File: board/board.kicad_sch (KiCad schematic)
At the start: 34 parts, among them J1 Conn_01x10_Pin, J2 Conn_01x10, J4 Conn_01x02, J5 Conn_01x06, J6 Conn_01x04, J7 Conn_01x30, U2 nPM1300-QEAA, U3 MDBT50Q-P1MV2, Y1 32k Hz

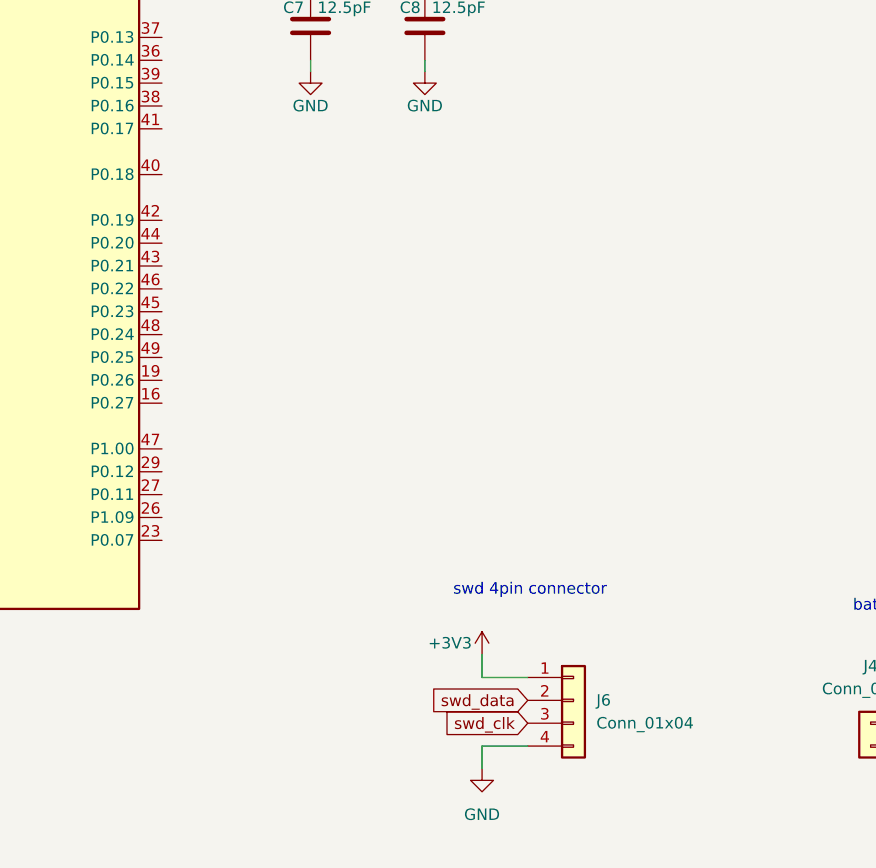
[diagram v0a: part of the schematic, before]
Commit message: board: sch fix swd connect with new footprint
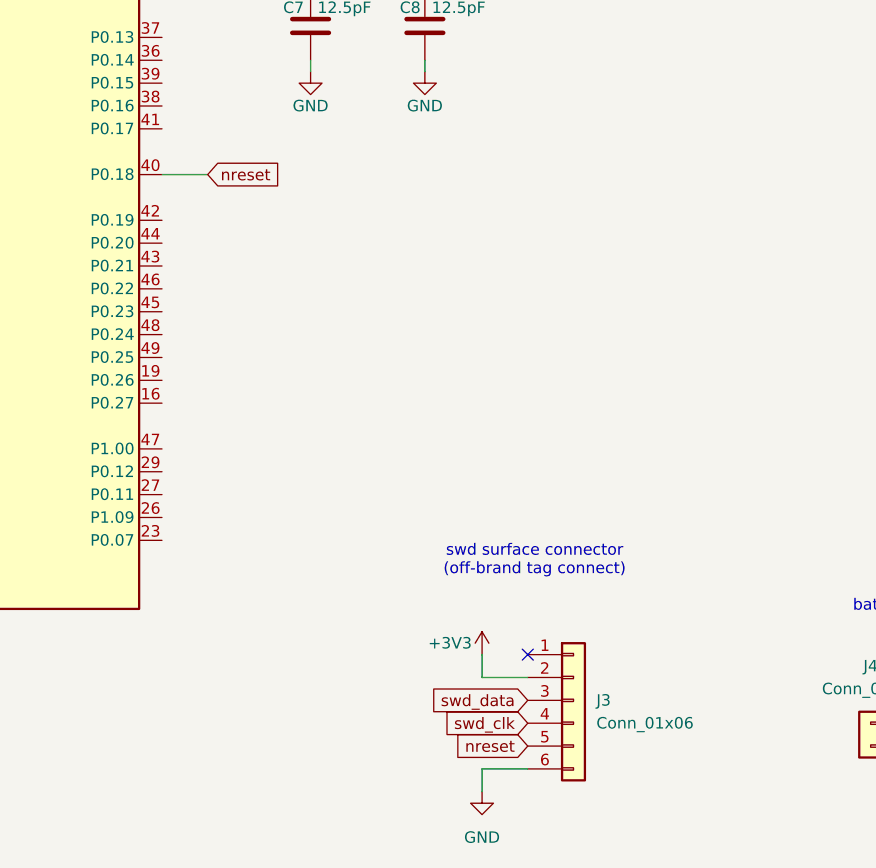
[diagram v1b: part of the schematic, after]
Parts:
- removed J6: Conn_01x04, symbol Connector_Generic:Conn_01x04
- added J3: Conn_01x06, phiboard:swd_pad, symbol Connector_Generic:Conn_01x06
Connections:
- net +3V3: now also J3.2 (Pin_2)
- net GND: now also J3.6 (Pin_6)
- net swd_clk: now also J3.4 (Pin_4)
- net swd_data: now also J3.3 (Pin_3)
- net nreset: now reaches U3.40 (P0.18)
- net nreset: now also J3.5 (Pin_5)
- no-connect marks 12 -> 13
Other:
- note added: "swd surface connector (off-brand tag connect)"
- note removed: "swd 4pin connector"
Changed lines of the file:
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@@
 		)
 	)
-	(text "swd 4pin connector"
+	(text "swd surface connector\n(off-brand tag connect)"
 		(exclude_from_sim no)
-		(at 164.084 250.698 0)
+		(at 164.592 247.396 0)
 		(effects
 			(font
@@
 	)
 	(no_connect
+		(at 163.83 257.81)
+	)
+	(no_connect
 		(at 290.83 53.34)
 	)
@@
 	(wire
 		(pts
+			(xy 128.27 204.47) (xy 123.19 204.47)
+		)
+		(stroke
+			(width 0)
+			(type default)
+		)
+	)
+	(wire
+		(pts
 			(xy 262.89 257.81) (xy 254 257.81)
 		)
@@
 	(wire
 		(pts
-			(xy 158.75 270.51) (xy 158.75 267.97)
+			(xy 158.75 273.05) (xy 158.75 270.51)
 		)
 		(stroke
@@
 	(wire
 		(pts
-			(xy 158.75 267.97) (xy 163.83 267.97)
+			(xy 158.75 270.51) (xy 163.83 270.51)
 		)
 		(stroke
@@
 		)
 	)
+	(global_label "nreset"
+		(shape input)
+		(at 128.27 204.47 0)
+		(fields_autoplaced yes)
+		(effects
+			(font
+				(size 1.27 1.27)
+			)
+			(justify left)
+		)
+		(property "Intersheetrefs" "${INTERSHEET_REFS}"
+			(at 137.1214 204.47 0)
+			(effects
+				(font
+					(size 1.27 1.27)
+				)
+				(justify left)
+				(hide yes)
+			)
+		)
+	)
 	(global_label "usbd-"
 		(shape input)
@@
 		)
 	)
+	(global_label "nreset"
+		(shape input)
+		(at 163.83 267.97 180)
+		(fields_autoplaced yes)
+		(effects
+			(font
+				(size 1.27 1.27)
+			)
+			(justify right)
+		)
+		(property "Intersheetrefs" "${INTERSHEET_REFS}"
+			(at 154.9786 267.97 0)
+			(effects
+				(font
+					(size 1.27 1.27)
+				)
+				(justify right)
+				(hide yes)
+			)
+		)
+	)
 	(global_label "sclk"
 		(shape input)
@@
 	)
 	(symbol
+		(lib_id "Connector_Generic:Conn_01x06")
+		(at 168.91 262.89 0)
+		(unit 1)
+		(exclude_from_sim no)
+		(in_bom yes)
+		(on_board yes)
+		(dnp no)
+		(fields_autoplaced yes)
+		(property "Reference" "J3"
+			(at 171.45 262.8899 0)
+			(effects
+				(font
+					(size 1.27 1.27)
+				)
+				(justify left)
+			)
+		)
+		(property "Value" "Conn_01x06"
+			(at 171.45 265.4299 0)
+			(effects
+				(font
+					(size 1.27 1.27)
+				)
+				(justify left)
+			)
+		)
+		(property "Footprint" "phiboard:swd_pad"
+			(at 168.91 262.89 0)
+			(effects
+				(font
+					(size 1.27 1.27)
+				)
+				(hide yes)
+			)
+		)
+		(property "Datasheet" "~"
+			(at 168.91 262.89 0)
+			(effects
+				(font
+					(size 1.27 1.27)
+				)
+				(hide yes)
+			)
+		)
+		(property "Description" "Generic connector, single row, 01x06, script generated (kicad-library-utils/schlib/autogen/connector/)"
+			(at 168.91 262.89 0)
+			(effects
+				(font
+					(size 1.27 1.27)
+				)
+				(hide yes)
+			)
+		)
+		(pin "4"
+		)
+		(pin "3"
+		)
+		(pin "2"
+		)
+		(pin "1"
+		)
+		(pin "6"
+		)
+		(pin "5"
+		)
+		(instances
+			(project ""
+				(path "/0bf1fdd4-5a89-4735-8383-190e40fb0179"
+					(reference "J3")
+					(unit 1)
+				)
+			)
+		)
+	)
+	(symbol
 		(lib_id "Device:LED")
 		(at 281.94 69.85 180)
@@
 	)
 	(symbol
-		(lib_id "Connector_Generic:Conn_01x04")
-		(at 168.91 262.89 0)
-		(unit 1)
-		(exclude_from_sim no)
-		(in_bom yes)
-		(on_board yes)
-		(dnp no)
-		(property "Reference" "J6"
-			(at 171.45 262.8899 0)
-			(effects
-				(font
-					(size 1.27 1.27)
-				)
-				(justify left)
-			)
-		)
-		(property "Value" "Conn_01x04"
-			(at 171.45 265.4299 0)
-			(effects
-				(font
-					(size 1.27 1.27)
-				)
-				(justify left)
-			)
-		)
-		(property "Footprint" ""
-			(at 168.91 262.89 0)
-			(effects
-				(font
-					(size 1.27 1.27)
-				)
-				(hide yes)
-			)
-		)
-		(property "Datasheet" "~"
-			(at 168.91 262.89 0)
-			(effects
-				(font
-					(size 1.27 1.27)
-				)
-				(hide yes)
-			)
-		)
-		(property "Description" "Generic connector, single row, 01x04, script generated (kicad-library-utils/schlib/autogen/connector/)"
-			(at 168.91 262.89 0)
-			(effects
-				(font
-					(size 1.27 1.27)
-				)
-				(hide yes)
-			)
-		)
-		(pin "3"
-		)
-		(pin "2"
-		)
-		(pin "4"
-		)
-		(pin "1"
-		)
-		(instances
-			(project ""
-				(path "/0bf1fdd4-5a89-4735-8383-190e40fb0179"
-					(reference "J6")
-					(unit 1)
-				)
-			)
-		)
-	)
-	(symbol
 		(lib_id "Device:R")
 		(at 283.21 83.82 90)
@@
 	(symbol
 		(lib_id "power:GND")
-		(at 158.75 270.51 0)
+		(at 158.75 273.05 0)
 		(unit 1)
 		(exclude_from_sim no)
@@
 		(fields_autoplaced yes)
 		(property "Reference" "#PWR024"
-			(at 158.75 276.86 0)
+			(at 158.75 279.4 0)
 			(effects
 				(font
@@
 		)
 		(property "Value" "GND"
-			(at 158.75 275.59 0)
+			(at 158.75 278.13 0)
 			(effects
 				(font
@@
 		)
 		(property "Footprint" ""
-			(at 158.75 270.51 0)
+			(at 158.75 273.05 0)
 			(effects
 				(font
@@
 		)
 		(property "Datasheet" ""
-			(at 158.75 270.51 0)
+			(at 158.75 273.05 0)
 			(effects
 				(font
@@
 		)
 		(property "Description" "Power symbol creates a global label with name \"GND\" , ground"
-			(at 158.75 270.51 0)
+			(at 158.75 273.05 0)
 			(effects
 				(font

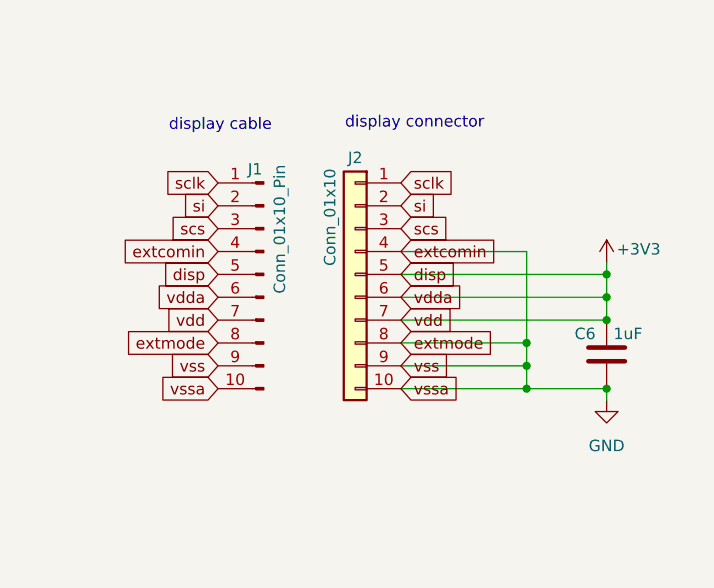
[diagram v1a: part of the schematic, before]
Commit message: board: sch tidy up display connector
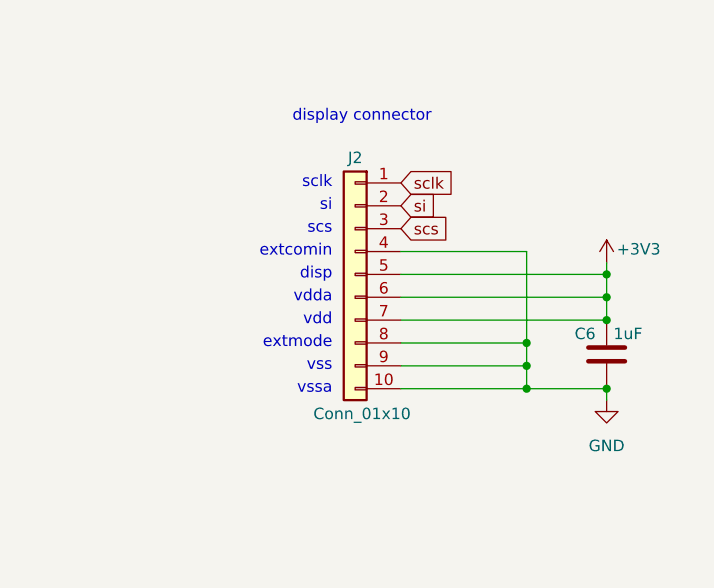
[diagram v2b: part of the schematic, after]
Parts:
- removed J1: Conn_01x10_Pin, symbol Connector:Conn_01x10_Pin
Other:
- note added: "disp"
- note added: "extcomin"
- note added: "extmode"
- note added: "sclk"
- note added: "scs"
- note added: "si"
- note added: "vdd"
- note added: "vdda"
- note added: "vss"
- note added: "vssa"
- note removed: "display cable"

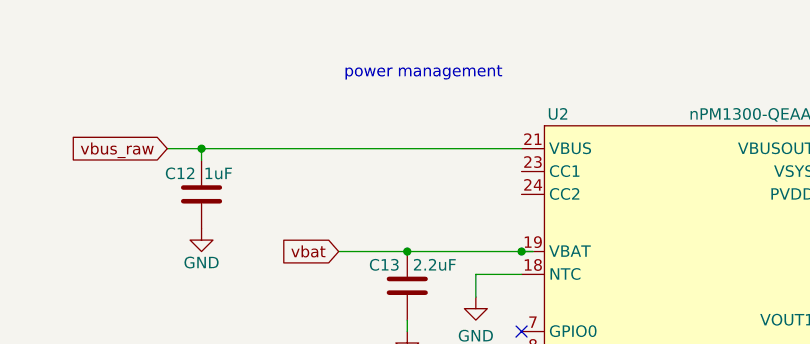
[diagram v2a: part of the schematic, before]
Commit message: board: sch assign display connector new ffc connector footprint and lcsc pn
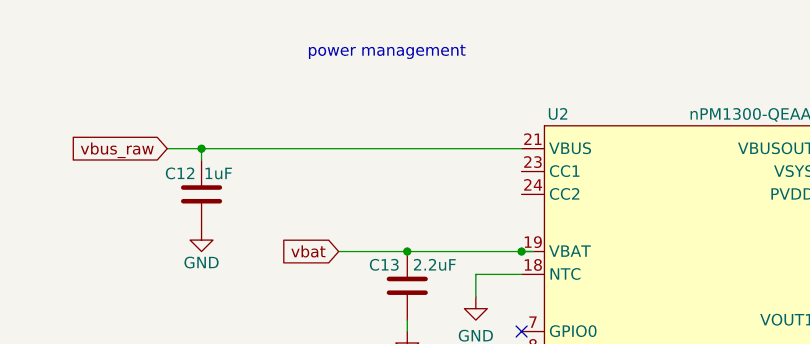
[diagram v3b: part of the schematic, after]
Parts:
- J2: footprint (none) -> phiboard:THD_0510-10CL-GF; LCSC PN (none) -> C283121
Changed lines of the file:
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@@
 	(text "power management"
 		(exclude_from_sim no)
-		(at 279.908 24.638 0)
+		(at 275.844 22.352 0)
 		(effects
 			(font
@@
 			)
 		)
-		(property "Footprint" ""
+		(property "Footprint" "phiboard:THD_0510-10CL-GF"
 			(at 59.69 46.99 0)
 			(effects
@@
 			(at 59.69 46.99 0)
 			(effects
+				(font
+					(size 1.27 1.27)
+				)
+				(hide yes)
+			)
+		)
+		(property "LCSC PN" "C283121"
+			(at 59.69 46.99 0)
+			(effects

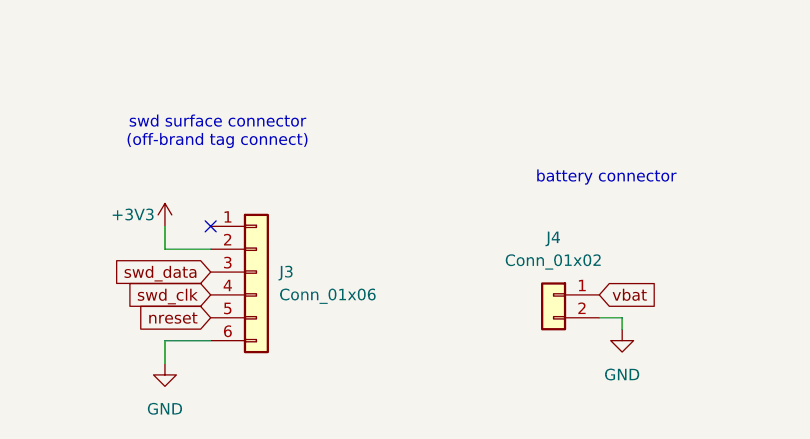
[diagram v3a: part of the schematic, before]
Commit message: board: sch assign footprint to board to board connector
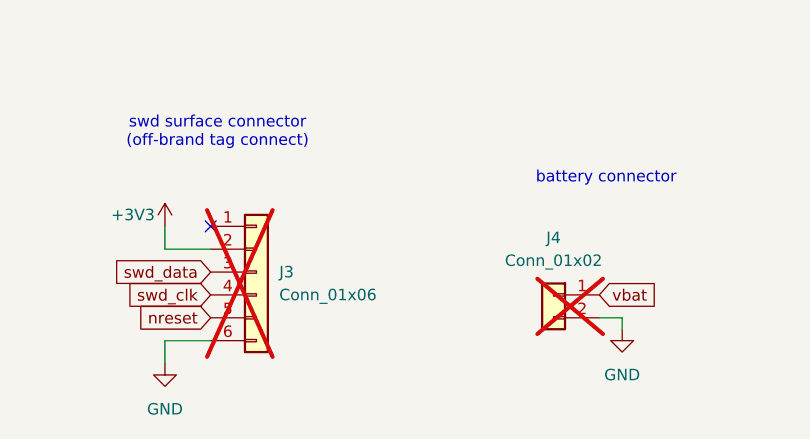
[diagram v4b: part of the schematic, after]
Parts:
- J3, J4: now not fitted; now left out of the parts list
- J7: footprint (none) -> phiboard:THD_0510-30CL-GF; JCSC PN (none) -> C283129
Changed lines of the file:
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@@
 		(unit 1)
 		(exclude_from_sim no)
-		(in_bom yes)
-		(on_board yes)
-		(dnp no)
+		(in_bom no)
+		(on_board no)
+		(dnp yes)
 		(fields_autoplaced yes)
 		(property "Reference" "J4"
@@
 			)
 		)
-		(property "Footprint" ""
+		(property "Footprint" "phiboard:THD_0510-30CL-GF"
 			(at 151.13 64.77 0)
 			(effects
@@
 			)
 		)
+		(property "JCSC PN" "C283129"
+			(at 151.13 64.77 90)
+			(effects
+				(font
+					(size 1.27 1.27)
+				)
+				(hide yes)
+			)
+		)
 		(pin "2"
 		)
@@
 		(unit 1)
 		(exclude_from_sim no)
-		(in_bom yes)
-		(on_board yes)
-		(dnp no)
+		(in_bom no)
+		(on_board no)
+		(dnp yes)
 		(fields_autoplaced yes)
 		(property "Reference" "J3"

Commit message: board: sch add footprint and lcsc pn to npm1300
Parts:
- U2: footprint (none) -> phiboard:nordic_npm1300-QEAA_qfn; LCSC PN (none) -> C7466043
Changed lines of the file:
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@@
 			)
 		)
-		(property "Footprint" ""
+		(property "Footprint" "phiboard:nordic_npm1300-QEAA_qfn"
 			(at 308.61 66.04 0)
 			(effects
@@
 			(at 308.61 66.04 0)
 			(effects
+				(font
+					(size 1.27 1.27)
+				)
+				(hide yes)
+			)
+		)
+		(property "LCSC PN" "C7466043"
+			(at 308.61 66.04 0)
+			(effects

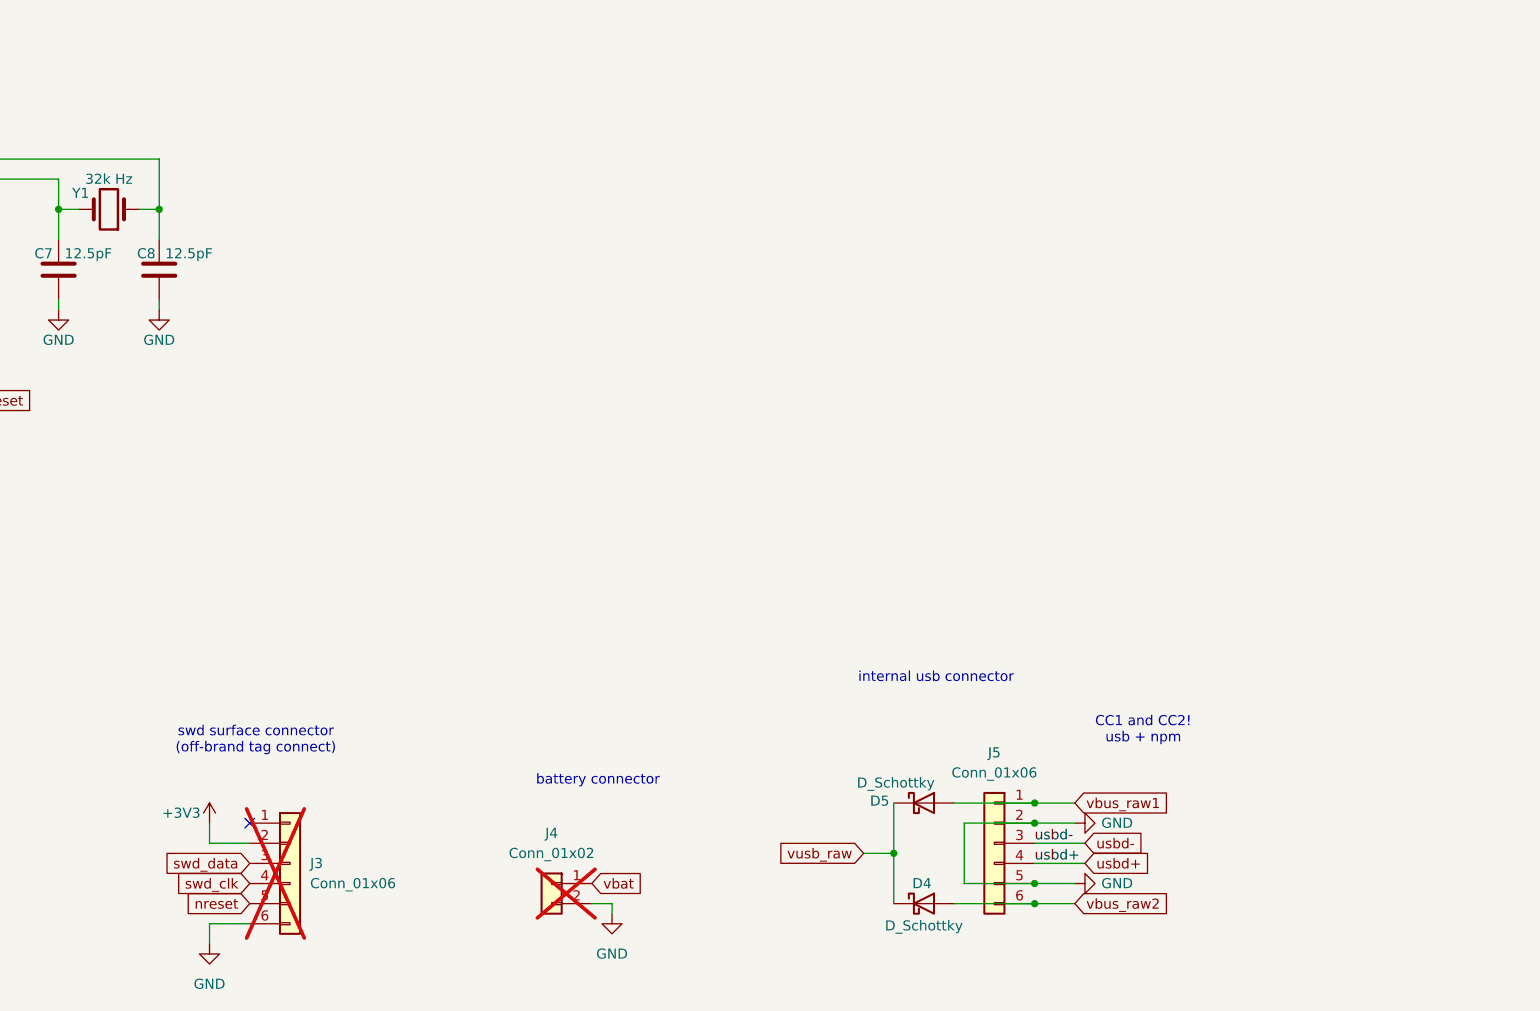
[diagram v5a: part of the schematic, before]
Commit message: board: sch add battery pad
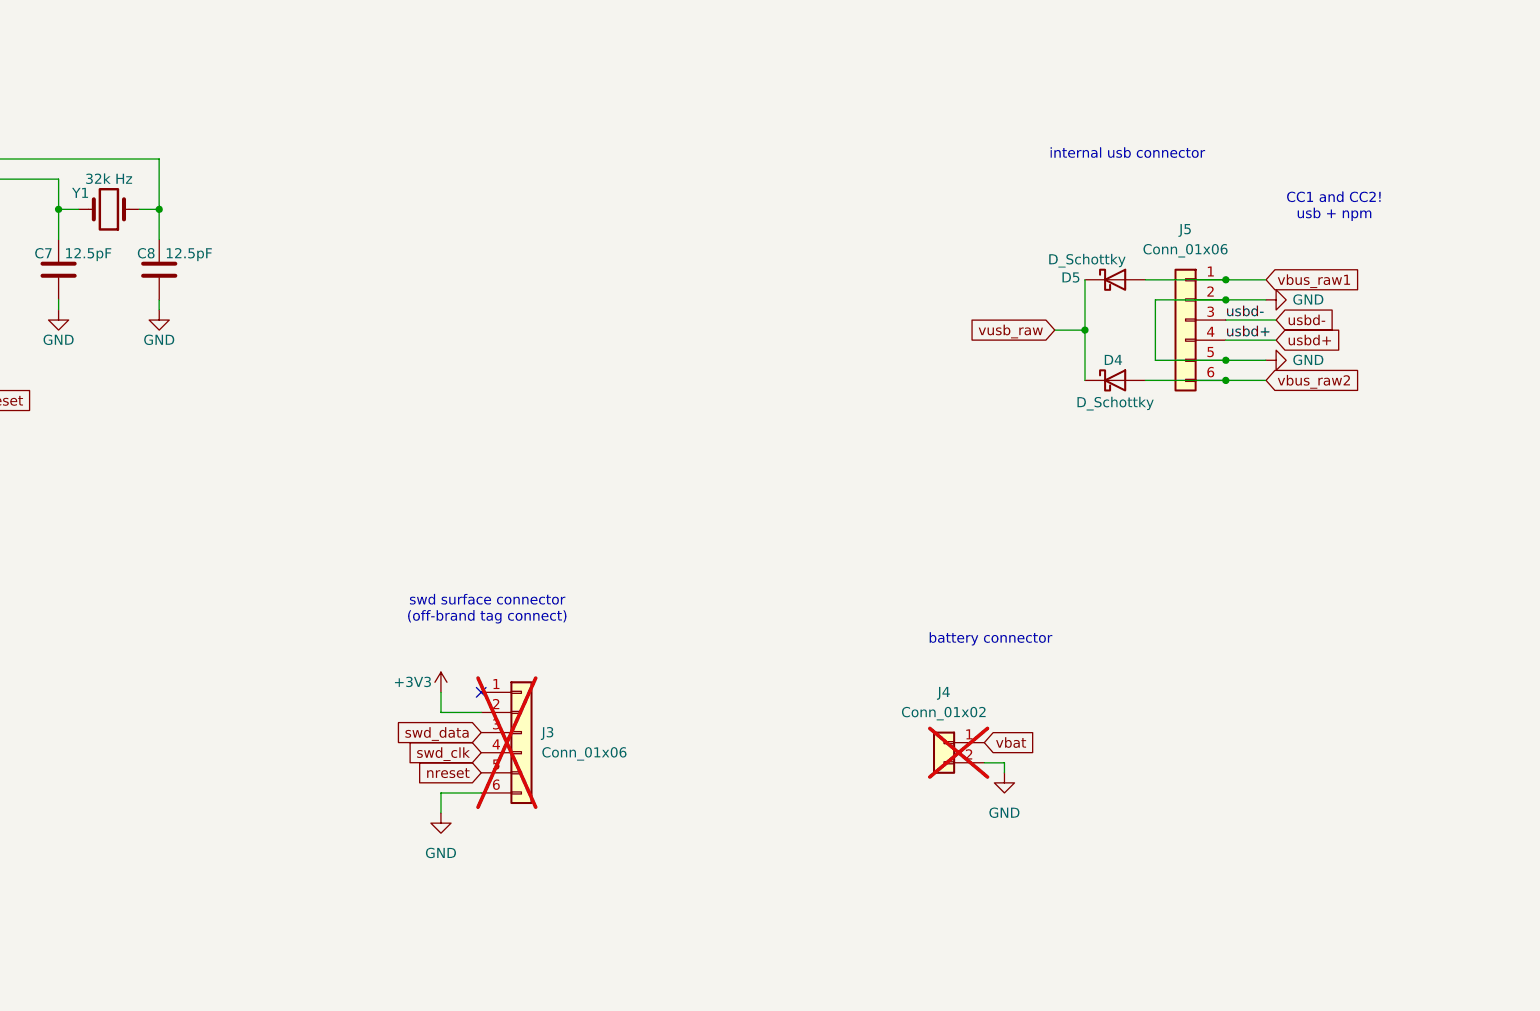
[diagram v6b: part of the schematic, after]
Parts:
- J4: footprint (none) -> Connector_PinHeader_2.54mm:PinHeader_1x02_P2.54mm_Vertical
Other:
- moved on the sheet: D4, D5, J3, J4, J5
